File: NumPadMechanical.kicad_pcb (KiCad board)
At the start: 2 copper layers, 108 x 74.5 mm, 35 parts, among them SW1 Push_Button, SW10 Push_Button, SW11 Push_Button, SW12 Push_Button, SW13 Push_Button, SW14 Push_Button, SW15 Push_Button, SW16 Push_Button, SW17 Push_Button, SW2 Push_Button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

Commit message: Se añaden diodos a la matriz de switches, se agrega conector usb y se coloca su cableado
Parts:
- removed SW1, SW10, SW11, SW12, SW13, SW14, SW15, SW16, SW17, SW2, SW3, SW4, SW5, SW6, SW7, SW8, SW9: Push_Button, Button_Switch_THT:SW_PUSH_6mm
- added D96: 1N5819, Diode_SMD:D_SOD-123, F.Cu at (357.2, 147.9)
- added J1: USB_C_Receptacle_USB2.0_14P, Connector_USB:USB_C_Receptacle_XKB_U262-16XN-4BVC11, F.Cu at (320.0, 137.5)
- added MX1: MX-NoLED, MX_Alps_Hybrid:MX-1U-NoLED, F.Cu at (38.1, 38.1)
- added MX10: MX-NoLED, MX_Alps_Hybrid:MX-1U-NoLED, F.Cu at (57.1, 76.2)
- added MX11: MX-NoLED, MX_Alps_Hybrid:MX-1U-NoLED, F.Cu at (76.2, 76.2)
- added MX12: MX-NoLED, MX_Alps_Hybrid:MX-1U-NoLED, F.Cu at (38.1, 95.2)
- added MX13: MX-NoLED, MX_Alps_Hybrid:MX-1U-NoLED, F.Cu at (57.1, 95.2)
- added MX14: MX-NoLED, MX_Alps_Hybrid:MX-1U-NoLED, F.Cu at (76.2, 95.2)
- added MX15: MX-NoLED, MX_Alps_Hybrid:MX-2U-NoLED, F.Cu at (95.2, 104.8)
- added MX16: MX-NoLED, MX_Alps_Hybrid:MX-2U-NoLED, F.Cu at (47.6, 114.3)
- added MX17: MX-NoLED, MX_Alps_Hybrid:MX-1U-NoLED, F.Cu at (76.2, 114.3)
- added MX2: MX-NoLED, MX_Alps_Hybrid:MX-1U-NoLED, F.Cu at (57.1, 38.1)
- added MX3: MX-NoLED, MX_Alps_Hybrid:MX-1U-NoLED, F.Cu at (76.2, 38.1)
- added MX4: MX-NoLED, MX_Alps_Hybrid:MX-1U-NoLED, F.Cu at (95.2, 38.1)
- added MX5: MX-NoLED, MX_Alps_Hybrid:MX-1U-NoLED, F.Cu at (38.1, 57.1)
- added MX6: MX-NoLED, MX_Alps_Hybrid:MX-1U-NoLED, F.Cu at (57.1, 57.1)
- added MX7: MX-NoLED, MX_Alps_Hybrid:MX-1U-NoLED, F.Cu at (76.2, 57.1)
- added MX8: MX-NoLED, MX_Alps_Hybrid:MX-2U-NoLED, F.Cu at (95.2, 66.7)
- added MX9: MX-NoLED, MX_Alps_Hybrid:MX-1U-NoLED, F.Cu at (38.1, 76.2)
- added R1: 22R, Resistor_SMD:R_0603_1608Metric_Pad0.98x0.95mm_HandSolder, F.Cu at (352.1, 147.5)
- added R2: 22R, Resistor_SMD:R_0603_1608Metric_Pad0.98x0.95mm_HandSolder, F.Cu at (352.1, 150.0)
- added R3: 5K, Resistor_SMD:R_0603_1608Metric_Pad0.98x0.95mm_HandSolder, F.Cu at (352.1, 152.5)
- added R4: 5K, Resistor_SMD:R_0603_1608Metric_Pad0.98x0.95mm_HandSolder, F.Cu at (352.1, 155.0)
- D1, D10, D11, D12, D13, D14, D15, D16, D17, D2, D3, D4, D5, D6, D7, D8, D9: value 1N4148 -> 1N4148W; footprint Diode_THT:D_DO-35_SOD27_P7.62mm_Horizontal -> Diode_SMD:D_SOD-123; moved to B.Cu
- U1: value STM32F103C8Tx -> STM32F103CBTx
- moved U1 63.5 mm to (127.5, 53.0)
- moved D12 58.7 mm to (38.1, 95.2)
- moved D9 56.6 mm to (38.1, 76.2)
- moved D5 55.8 mm to (38.1, 57.1)
- moved D1 55.5 mm to (38.1, 38.1)
- moved D16 51.9 mm to (47.6, 114.3)
- moved D13 39.7 mm to (57.1, 95.2)
- moved D10 37.2 mm to (57.1, 76.2)
- moved D2 36.6 mm to (57.1, 38.1)
- moved D6 36.6 mm to (57.1, 57.1)
- moved D17 26.8 mm to (76.2, 114.3)
- moved D14 21.2 mm to (76.2, 95.2)
- moved D3 18.5 mm to (76.2, 38.1)
- moved D15 18.0 mm to (95.2, 104.8)
- moved D11 17.8 mm to (76.2, 76.2)
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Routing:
- net COL1: track 0.00 -> 160.3 mm
- net COL3: track 0.00 -> 152.4 mm
- net COL4: track 0.00 -> 133.4 mm
- net COL2: track 0.00 -> 114.3 mm
- removed copper zone on F.Cu, net unconnected-(U1-VDD-Pad36)
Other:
- board outline removed

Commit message: Se modifican huellas de dispositivos y se agregan modelos 3d en algunas de las huellas
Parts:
- D1, D10, D11, D12, D13, D14, D15, D16, D17, D2, D3, D4, D5, D6, D7, D8, D9: footprint Diode_SMD:D_SOD-123 -> D_SOD-123_A:D_SOD-123_A
- D96: footprint Diode_SMD:D_SOD-123 -> D_SOD-123_A:D_SOD-123_A; moved to B.Cu
- J1, R1, R2, R3, R4, U1: moved to B.Cu
- MX15, MX8: footprint MX_Alps_Hybrid:MX-2U-NoLED -> MX_Alps_Hybrid:MX-Alps-Hybrid-2U-Vertical
- moved D96 300.9 mm to (81.0, 28.5), turned to 180 degrees
- moved R1 291.6 mm to (86.1, 28.1), turned to 180 degrees
- moved R2 291.6 mm to (86.1, 30.6), turned to 180 degrees
- moved R3 291.6 mm to (86.1, 33.1), turned to 180 degrees
- moved R4 291.6 mm to (86.1, 35.6), turned to 180 degrees
- moved J1 276.4 mm to (67.1, 25.9)
- moved U1 33.1 mm to (94.5, 51.0), turned to 180 degrees
- moved D1 4.95 mm to (41.6, 41.6)
- moved D10 4.95 mm to (60.6, 79.7)
- moved D11 4.95 mm to (79.7, 79.7)
- moved D12 4.95 mm to (41.6, 98.8)
- moved D13 4.95 mm to (60.6, 98.8)
- moved D14 4.95 mm to (79.7, 98.8)
- moved D15 4.95 mm to (98.8, 108.3)
- moved D16 4.95 mm to (51.1, 117.8)
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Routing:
- net COL1: track 160.3 -> 0.00 mm
- net COL3: track 152.4 -> 0.00 mm
- net COL4: track 133.4 -> 0.00 mm
- net COL2: track 114.3 -> 0.00 mm
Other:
- board outline added: 86.4 x 106 mm

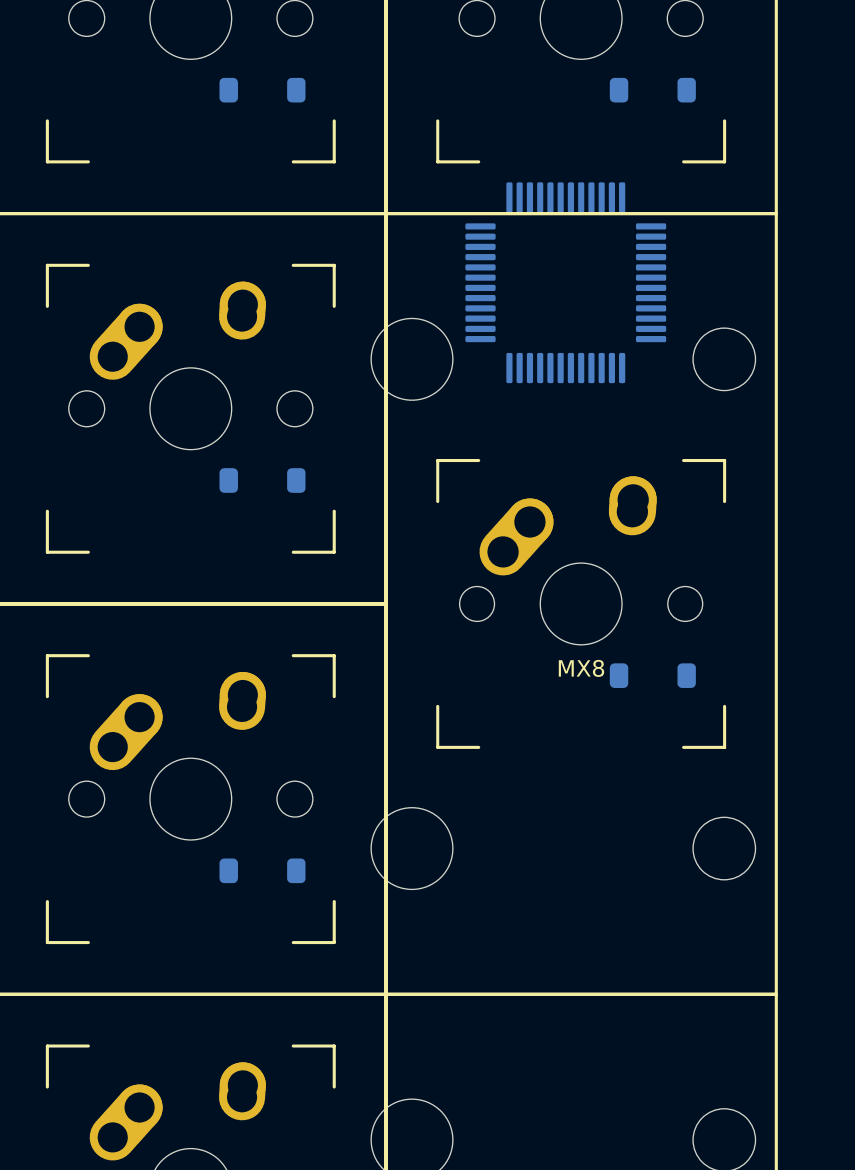
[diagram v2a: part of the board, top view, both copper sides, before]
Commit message: Agregados capacitores de acoplamiento y regulador de 3v3
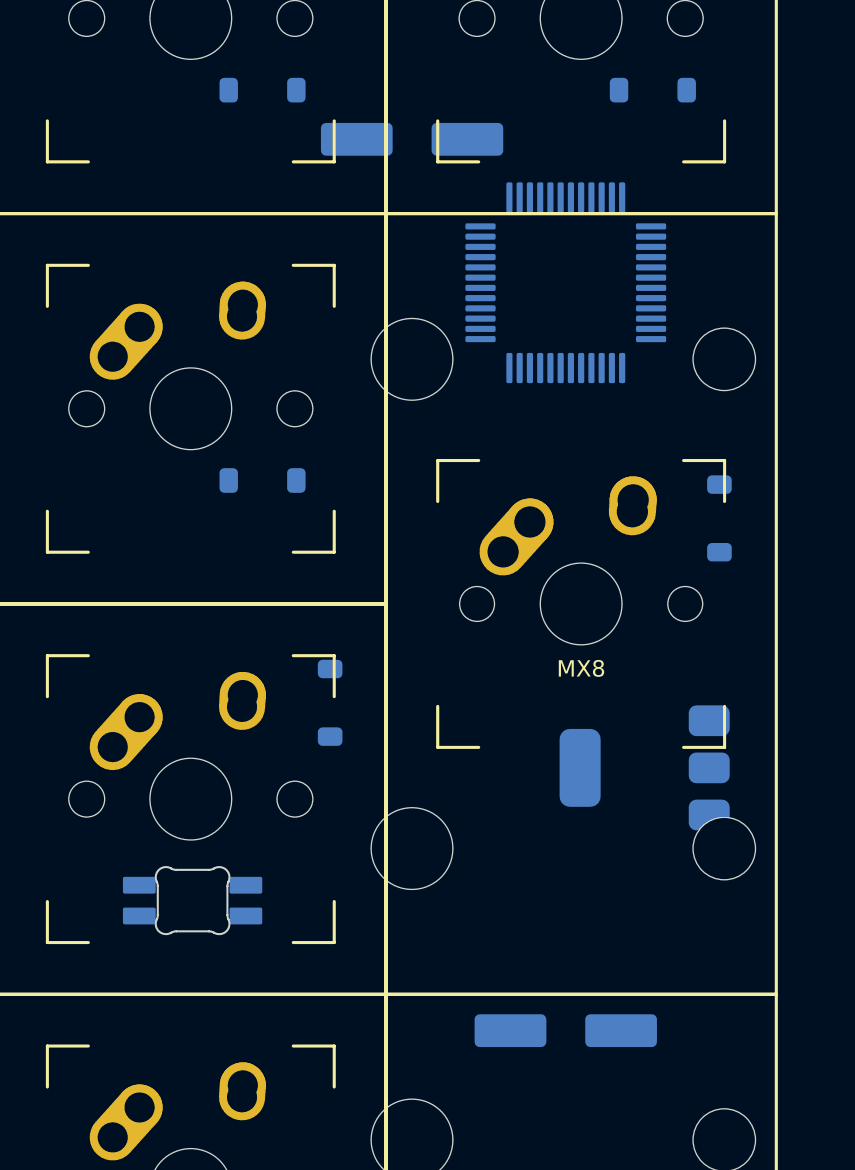
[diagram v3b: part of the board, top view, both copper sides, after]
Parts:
- added C1: 1uF, Capacitor_SMD:CP_Elec_6.3x7.7, B.Cu at (87.0, 44.0)
- added C2: 1uF, Capacitor_SMD:CP_Elec_6.3x7.7, B.Cu at (94.5, 87.5)
- added D18: SK6812MINI-E, kicad-keyboard-parts:MX_SK6812MINI-E, F.Cu at (76.3, 76.1)
- added U2: AMS1117-3.3, Package_TO_SOT_SMD:SOT-223-3_TabPin2, B.Cu at (98.3, 74.7)
- moved D11 8.84 mm to (83.0, 71.5), turned to 90 degrees
- moved D8 8.33 mm to (102.0, 62.5), turned to 90 degrees

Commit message: Agregado cristal oscilador y corregido el conector usb, se agregan footprints de algunos dispositivos
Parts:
- added C11: 100nF, Capacitor_SMD:C_0603_1608Metric_Pad1.08x0.95mm_HandSolder, B.Cu at (53.9, 50.7)
- added C12: 20pF, Capacitor_SMD:C_0603_1608Metric_Pad1.08x0.95mm_HandSolder, B.Cu at (53.9, 53.2)
- added C13: 20pF, Capacitor_SMD:C_0603_1608Metric_Pad1.08x0.95mm_HandSolder, B.Cu at (99.1, 46.5)
- added C3: 100nF, Capacitor_SMD:C_0603_1608Metric_Pad1.08x0.95mm_HandSolder, B.Cu at (53.9, 40.6)
- added C4: 100nF, Capacitor_SMD:C_0603_1608Metric_Pad1.08x0.95mm_HandSolder, B.Cu at (53.9, 43.1)
- added C5: 100nF, Capacitor_SMD:C_0603_1608Metric_Pad1.08x0.95mm_HandSolder, B.Cu at (53.9, 45.6)
- added C6: 100nF, Capacitor_SMD:C_0603_1608Metric_Pad1.08x0.95mm_HandSolder, B.Cu at (53.9, 48.2)
- added R5: 10K, Resistor_SMD:R_0603_1608Metric_Pad0.98x0.95mm_HandSolder, B.Cu at (61.4, 47.0)
- added Y1: Crystal, Crystal:Crystal_SMD_HC49-SD_HandSoldering, B.Cu at (41.0, 42.5)
- moved U2 24.9 mm to (97.8, 99.6)
- moved D16 23.8 mm to (53.9, 141.4)
- moved D17 23.8 mm to (82.5, 141.4)
- moved MX16 23.8 mm to (50.4, 137.9)
- moved MX17 23.8 mm to (79.0, 137.9)
- moved D1 23.8 mm to (44.4, 65.2)
- moved D2 23.8 mm to (63.5, 65.2)
- moved D3 23.8 mm to (82.5, 65.2)
- moved D4 23.8 mm to (101.6, 65.2)
- moved D5 23.8 mm to (44.4, 84.2)
- moved D6 23.8 mm to (63.5, 84.2)
- moved D7 23.8 mm to (82.5, 84.2)
- moved MX5 23.8 mm to (40.9, 80.7)
- moved MX6 23.8 mm to (60.0, 80.7)
- moved MX7 23.8 mm to (79.0, 80.7)
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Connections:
- C1 pad 2: Net-(U2-GND) -> GND
- C2 pad 2: Net-(U2-GND) -> GND
- D96 pad 1: 5V -> +5V
- R1 pad 2: D- -> USB_D-
- R2 pad 2: D+ -> USB_D+
- U1 pad 1: unconnected-(U1-VBAT-Pad1) -> +3.3V
- U1 pad 23: Net-(U1-VSS-Pad23) -> GND
- U1 pad 24: unconnected-(U1-VDD-Pad24) -> +3.3V
- U1 pad 32: unconnected-(U1-PA11-Pad32) -> USB_D-
- U1 pad 33: unconnected-(U1-PA12-Pad33) -> USB_D+
- U1 pad 34: unconnected-(U1-PA13-Pad34) -> SWDIO
- U1 pad 35: Net-(U1-VSS-Pad23) -> GND
- U1 pad 36: unconnected-(U1-VDD-Pad36) -> +3.3V
- U1 pad 37: unconnected-(U1-PA14-Pad37) -> SWCLK
- U1 pad 44: unconnected-(U1-BOOT0-Pad44) -> Net-(U1-BOOT0)
- U1 pad 47: Net-(U1-VSS-Pad23) -> GND
- U1 pad 48: unconnected-(U1-VDD-Pad48) -> +3.3V
- U1 pad 5: unconnected-(U1-PD0-Pad5) -> OSC_IN
- U1 pad 6: unconnected-(U1-PD1-Pad6) -> OSC_OUT
- U1 pad 7: unconnected-(U1-NRST-Pad7) -> Net-(C11-+)
- U1 pad 8: unconnected-(U1-VSSA-Pad8) -> GND
- U1 pad 9: unconnected-(U1-VDDA-Pad9) -> +3.3VA
- U2 pad 1: Net-(U2-GND) -> GND
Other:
- board size 86.4 x 106 mm -> 86.4 x 116.6 mm

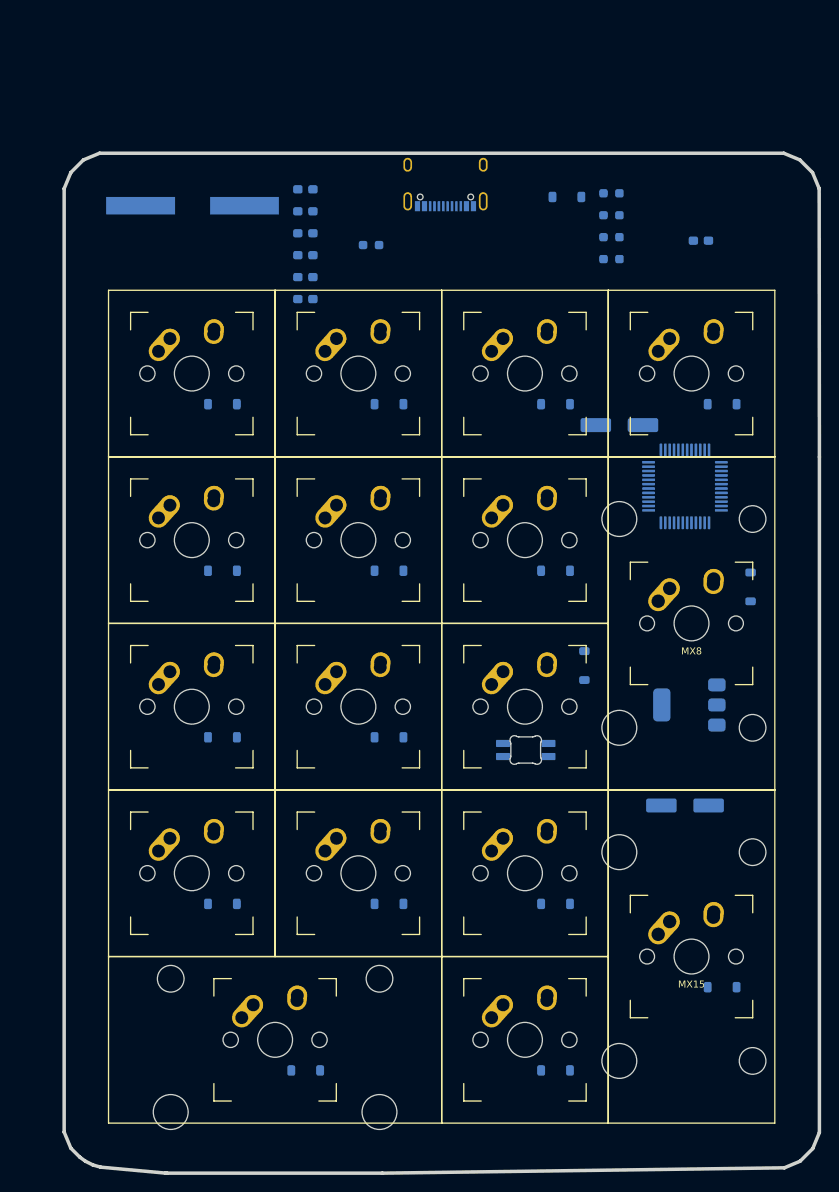
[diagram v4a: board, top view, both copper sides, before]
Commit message: Modificado el esquematico finalizando conexiones, se añaden leds rgb y de señalizacion, se agregan footprints de todos los elementos faltantes y se realiza acomodo de pcb preliminar
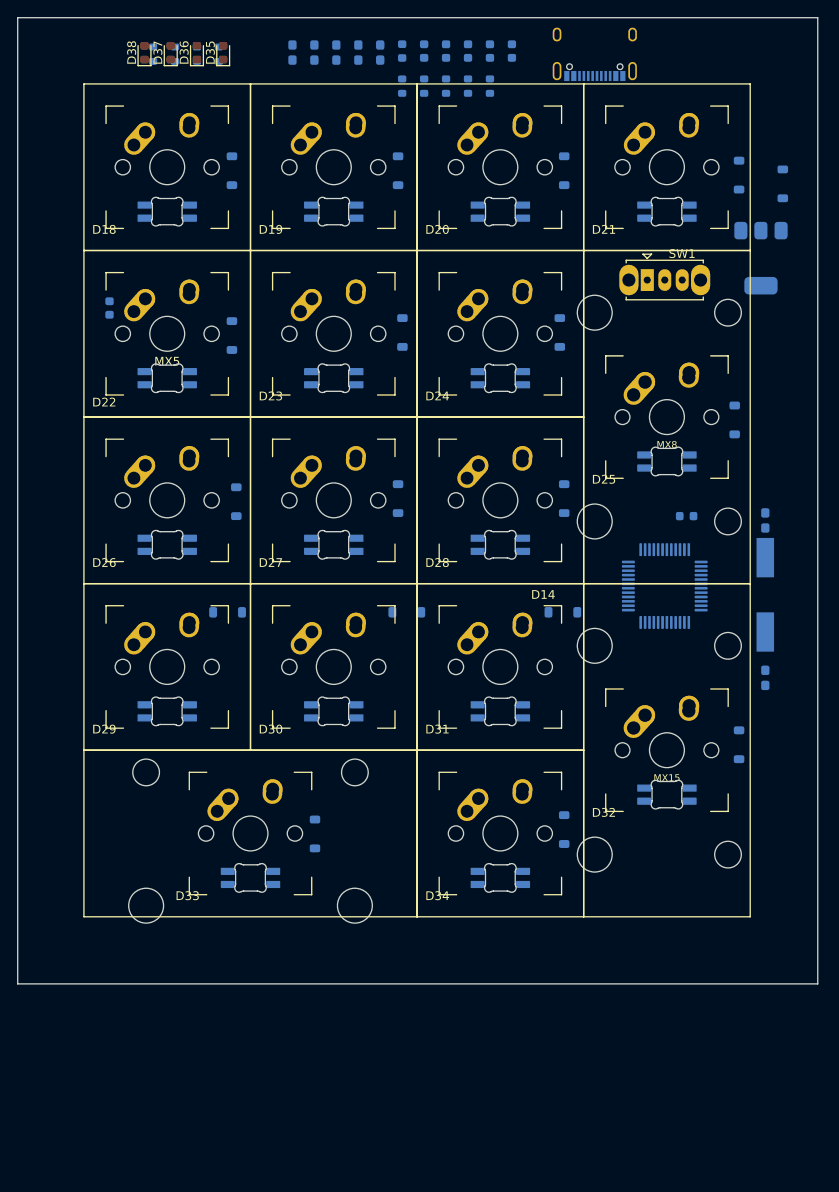
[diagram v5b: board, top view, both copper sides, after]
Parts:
- removed D96: 1N5819, D_SOD-123_A:D_SOD-123_A
- added C10: 10uF, Capacitor_SMD:C_0603_1608Metric, B.Cu at (67.5, 24.8)
- added C7: 10uF, Capacitor_SMD:C_0603_1608Metric, B.Cu at (75.0, 24.8)
- added C8: 10nF, Capacitor_SMD:C_0603_1608Metric, B.Cu at (72.5, 24.8)
- added C9: 10uF, Capacitor_SMD:C_0603_1608Metric, B.Cu at (70.0, 24.8)
- added D19: SK6812MINI-E, kicad-keyboard-parts:MX_SK6812MINI-E, F.Cu at (57.1, 38.1)
- added D20: SK6812MINI-E, kicad-keyboard-parts:MX_SK6812MINI-E, F.Cu at (76.2, 38.1)
- added D21: SK6812MINI-E, kicad-keyboard-parts:MX_SK6812MINI-E, F.Cu at (95.2, 38.1)
- added D22: SK6812MINI-E, kicad-keyboard-parts:MX_SK6812MINI-E, F.Cu at (38.1, 57.1)
- added D23: SK6812MINI-E, kicad-keyboard-parts:MX_SK6812MINI-E, F.Cu at (57.1, 57.1)
- added D24: SK6812MINI-E, kicad-keyboard-parts:MX_SK6812MINI-E, F.Cu at (76.2, 57.1)
- added D25: SK6812MINI-E, kicad-keyboard-parts:MX_SK6812MINI-E, F.Cu at (95.2, 66.7)
- added D26: SK6812MINI-E, kicad-keyboard-parts:MX_SK6812MINI-E, F.Cu at (38.1, 76.2)
- added D27: SK6812MINI-E, kicad-keyboard-parts:MX_SK6812MINI-E, F.Cu at (57.1, 76.2)
- added D28: SK6812MINI-E, kicad-keyboard-parts:MX_SK6812MINI-E, F.Cu at (76.2, 76.2)
- added D29: SK6812MINI-E, kicad-keyboard-parts:MX_SK6812MINI-E, F.Cu at (38.1, 95.2)
- added D30: SK6812MINI-E, kicad-keyboard-parts:MX_SK6812MINI-E, F.Cu at (57.1, 95.2)
- added D31: SK6812MINI-E, kicad-keyboard-parts:MX_SK6812MINI-E, F.Cu at (76.2, 95.2)
- added D32: SK6812MINI-E, kicad-keyboard-parts:MX_SK6812MINI-E, F.Cu at (95.2, 104.8)
- added D33: SK6812MINI-E, kicad-keyboard-parts:MX_SK6812MINI-E, F.Cu at (47.6, 114.3)
- added D34: SK6812MINI-E, kicad-keyboard-parts:MX_SK6812MINI-E, F.Cu at (76.2, 114.3)
- added D35: LED, LED_SMD:LED_0603_1608Metric, F.Cu at (44.5, 25.0)
- added D36: LED, LED_SMD:LED_0603_1608Metric, F.Cu at (41.5, 25.0)
- added D37: LED, LED_SMD:LED_0603_1608Metric, F.Cu at (38.5, 25.0)
- added D38: LED, LED_SMD:LED_0603_1608Metric, F.Cu at (35.5, 25.0)
- added D39: 1N5819, D_SOD-123_A:D_SOD-123_A, B.Cu at (108.5, 40.0)
- added F1: 500mA, Fuse:Fuse_0603_1608Metric, B.Cu at (65.0, 24.8)
- added FB1: 130R, Inductor_SMD:L_0603_1608Metric, B.Cu at (97.5, 78.0)
- added R6: 220R, Resistor_SMD:R_0603_1608Metric, B.Cu at (36.5, 25.2)
- added R7: 220R, Resistor_SMD:R_0603_1608Metric, B.Cu at (39.0, 25.2)
- added R8: 220R, Resistor_SMD:R_0603_1608Metric, B.Cu at (41.5, 25.2)
- added R9: 220R, Resistor_SMD:R_0603_1608Metric, B.Cu at (44.0, 25.2)
- added SW1: SW_SPDT, Button_Switch_THT:SW_Slide_SPDT_Straight_CK_OS102011MS2Q, F.Cu at (93.0, 51.0)
- C1, C2: value 1uF -> 10uF; footprint Capacitor_SMD:CP_Elec_6.3x7.7 -> Capacitor_SMD:C_0603_1608Metric
- R1, R2: value 22R -> 1K5; footprint Resistor_SMD:R_0603_1608Metric_Pad0.98x0.95mm_HandSolder -> Resistor_SMD:R_0603_1608Metric
- R3, R4, R5: footprint Resistor_SMD:R_0603_1608Metric_Pad0.98x0.95mm_HandSolder -> Resistor_SMD:R_0603_1608Metric
- U1: value STM32F103CBTx -> STM32F103CBT6
- Y1: footprint Crystal:Crystal_SMD_HC49-SD_HandSoldering -> Crystal:Crystal_SMD_HC49-SD
- moved C2 87.0 mm to (31.5, 54.2), turned to 90 degrees
- moved Y1 79.2 mm to (106.5, 87.0), turned to -90 degrees
- moved D18 74.0 mm to (38.1, 38.1)
- moved C12 58.4 mm to (106.5, 78.5), turned to 90 degrees
- moved U2 51.7 mm to (106.0, 48.5), turned to -90 degrees
- moved C13 50.5 mm to (106.5, 96.5), turned to -90 degrees
- moved C1 44.5 mm to (77.5, 24.8), turned to 90 degrees
- moved D13 33.4 mm to (65.5, 89.0), turned to 180 degrees
- moved D14 33.4 mm to (83.3, 89.0), turned to 180 degrees
- moved D12 33.4 mm to (45.0, 89.0), turned to 180 degrees
- moved R4 29.2 mm to (67.5, 28.8), turned to 90 degrees
- moved D15 27.8 mm to (103.5, 104.2), turned to -90 degrees
- moved D17 27.6 mm to (83.5, 113.8), turned to 90 degrees
- moved D10 27.3 mm to (64.5, 76.0), turned to 90 degrees
- moved D6 27.3 mm to (65.0, 57.0), turned to 90 degrees
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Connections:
- net 5V renamed VBUS
- C2 pad 1: 3V3 -> +3.3V
- D18 pad 1: unconnected-(D18-VDD-Pad1) -> +3V3
- D18 pad 2: unconnected-(D18-DOUT-Pad2) -> Net-(D18-DOUT)
- D18 pad 3: unconnected-(D18-VSS-Pad3) -> GND
- D18 pad 4: unconnected-(D18-DIN-Pad4) -> LEDPIN
- J1 pad A6: Net-(J1-D+-PadA6) -> USB_D+
- J1 pad A7: Net-(J1-D--PadA7) -> USB_D-
- J1 pad B6: Net-(J1-D+-PadA6) -> USB_D+
- J1 pad B7: Net-(J1-D--PadA7) -> USB_D-
- R1 pad 1: Net-(J1-D--PadA7) -> USB_D-
- R1 pad 2: USB_D- -> +3.3V
- R2 pad 1: Net-(J1-D+-PadA6) -> USB_D+
- R2 pad 2: USB_D+ -> +3.3V
- U1 pad 10: unconnected-(U1-PA0-Pad10) -> COL1
- U1 pad 11: unconnected-(U1-PA1-Pad11) -> COL2
- U1 pad 12: unconnected-(U1-PA2-Pad12) -> COL3
- U1 pad 13: unconnected-(U1-PA3-Pad13) -> COL4
- U1 pad 14: unconnected-(U1-PA4-Pad14) -> ROW1
- U1 pad 15: unconnected-(U1-PA5-Pad15) -> ROW2
- U1 pad 16: unconnected-(U1-PA6-Pad16) -> ROW3
- U1 pad 17: unconnected-(U1-PA7-Pad17) -> ROW4
- U1 pad 18: unconnected-(U1-PB0-Pad18) -> LED1
- U1 pad 19: unconnected-(U1-PB1-Pad19) -> LED2
- U1 pad 20: unconnected-(U1-PB2-Pad20) -> LED3
- U1 pad 29: unconnected-(U1-PA8-Pad29) -> ROW5
- U1 pad 30: unconnected-(U1-PA9-Pad30) -> LEDPIN
- U1 pad 39: unconnected-(U1-PB3-Pad39) -> LED4
- U2 pad 2: 3V3 -> +3.3V
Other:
- board size 86.4 x 116.6 mm -> 91.5 x 110.5 mm
